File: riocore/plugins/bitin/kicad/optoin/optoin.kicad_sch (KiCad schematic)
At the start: 6 parts, among them J1 opto_in, U1 LTV-817S

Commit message: generator: new top secret feature :)
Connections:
- net IN renamed bit
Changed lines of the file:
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@@
 		)
 	)
-	(hierarchical_label "IN"
+	(hierarchical_label "bit"
 		(shape input)
 		(at 115.57 95.25 180)

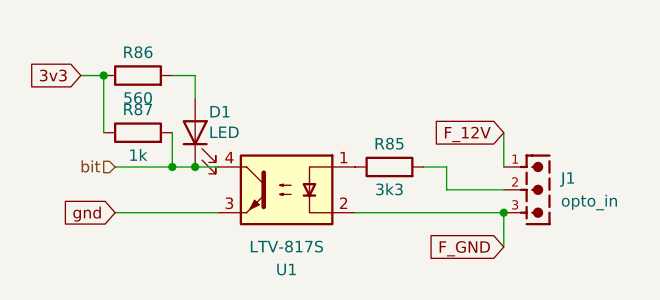
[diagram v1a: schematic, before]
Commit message: kicad: get power-signals
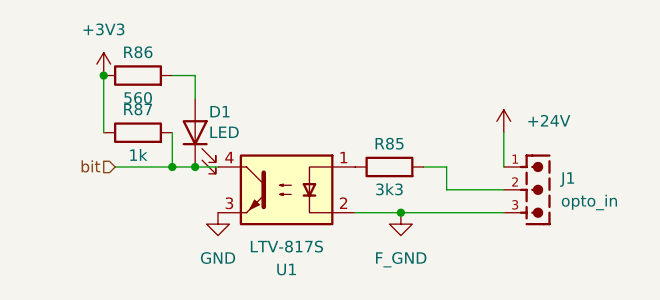
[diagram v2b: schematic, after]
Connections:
- net 3v3 renamed +3V3
- net F_12V renamed +24V
- net gnd renamed GND
